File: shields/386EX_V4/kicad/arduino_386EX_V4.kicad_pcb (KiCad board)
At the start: 2 copper layers, 93.3 x 60.3 mm, 50 parts, among them J1 Conn_01x02_Pin, J2 JTAG, J3 Conn_01x04_Pin, J4 Conn_01x04_Pin, J5 Conn_01x04_Pin, J6 SERIAL0, J9 WP Jumper, U1 AT24CS01-STUM, U11 I386EX_PQFP, U2 ULN2003A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

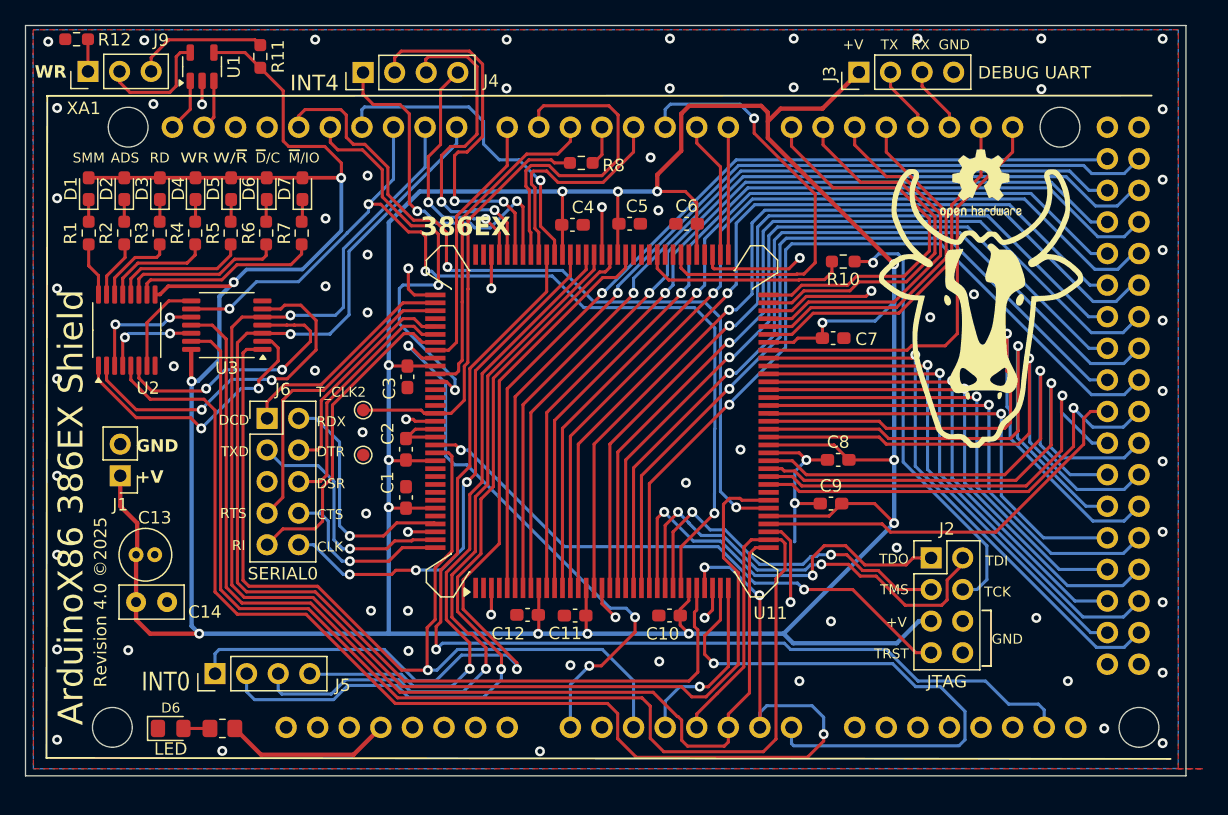
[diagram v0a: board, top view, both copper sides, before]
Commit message: 386EX_V4 updated to V5 with 4-layer PCB.
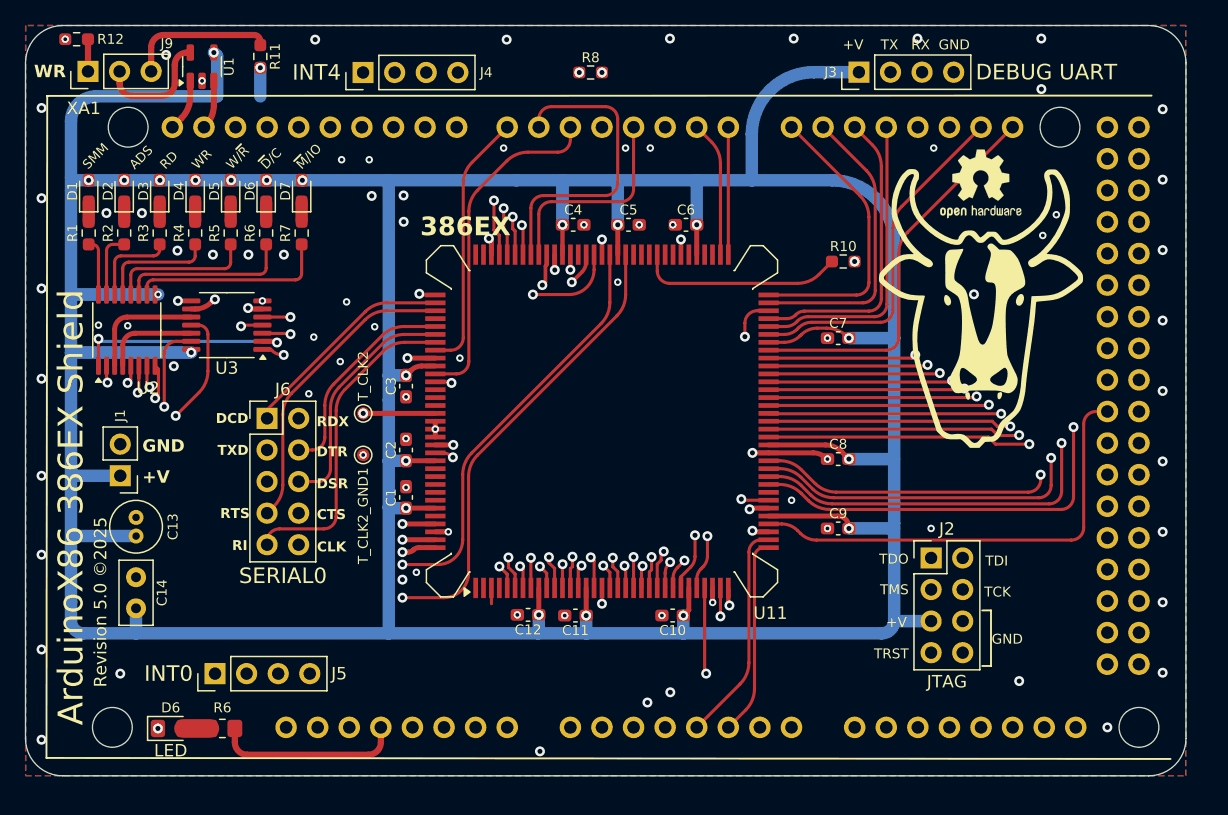
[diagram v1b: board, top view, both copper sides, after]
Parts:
- moved R8 7.31 mm to (155.9, 67.9)
- moved C9 2.08 mm to (175.8, 104.6)
- moved C13 1.50 mm to (119.4, 105.2), turned to 90 degrees
- moved C3 0.76 mm to (141.1, 93.1)
- moved C14 0.50 mm to (119.4, 111.0), turned to 90 degrees
- moved C7 0.40 mm to (175.8, 89.3), turned to 0 degrees
- moved T_CLK2 0.26 mm to (137.6, 95.3)
- moved C10 0.25 mm to (162.5, 111.6)
- moved D7 0.21 mm to (132.7, 77.4)
- moved D6 0.21 mm to (129.8, 77.4)
- moved D5 0.20 mm to (127.0, 77.4)
- moved D4 0.20 mm to (124.1, 77.4)
- moved D3 0.20 mm to (121.3, 77.4)
- moved D2 0.20 mm to (118.4, 77.4)
- moved D1 0.20 mm to (115.6, 77.4)
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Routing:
- net ~{ADS}: track 110.4 -> 61.5 mm, vias 1 -> 3
- net GND: track 68.2 -> 24.0 mm, vias 76 -> 86
- net ~{READY}: track 46.5 -> 13.5 mm
- net D/~{C}: track 95.5 -> 64.3 mm, vias 1 -> 3
- net ~{SMIACT}: track 79.3 -> 51.3 mm, vias 1 -> 2
- net ~{SMI}: track 35.3 -> 10.7 mm
- net NMI: track 88.2 -> 66.6 mm
- net W/~{R}: track 106.2 -> 86.3 mm, vias 3 -> 2
- net ~{WR}: track 109.6 -> 91.8 mm, vias 0 -> 2
- net INT0: track 69.7 -> 54.4 mm
- net INT1: track 64.6 -> 49.5 mm
- net M/~{IO}: track 80.8 -> 67.4 mm, vias 4 -> 3
- net /A4_A: track 41.5 -> 28.8 mm
- net /A7_A: track 49.3 -> 37.3 mm
- net /A5_A: track 45.4 -> 33.6 mm
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- added copper zone on In1.Cu, net GND
- added copper zone on In2.Cu, net GND
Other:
- outline, holes or cut-outs redrawn
- copper layers 2 -> 4
- board text added: "Revision 5.0 ©2025"
- board text removed: "Revision 4.0 ©2025"
